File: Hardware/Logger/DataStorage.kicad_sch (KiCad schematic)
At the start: 10 parts, among them J6 112K-TAA0-RA1_ATTEND

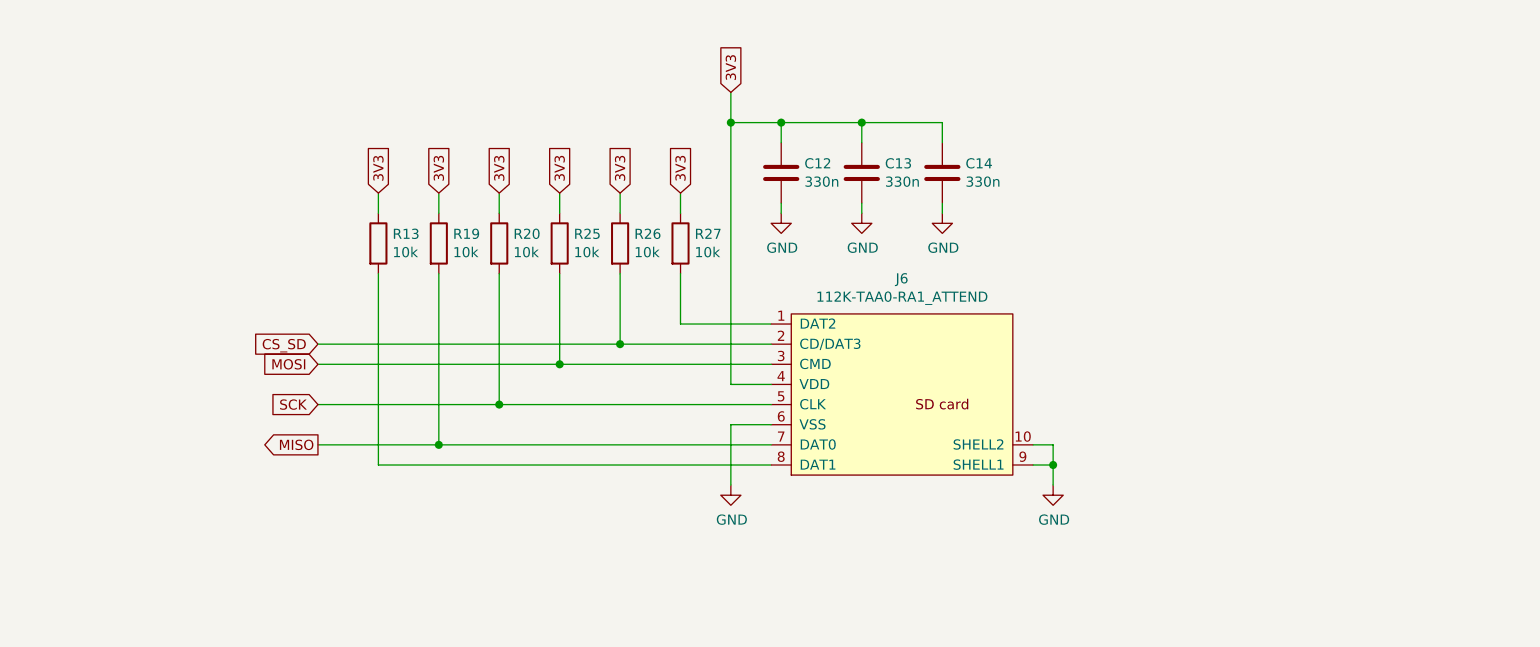
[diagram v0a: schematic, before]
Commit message: fixed SPI connections to SD card, added ESD protection for SD card
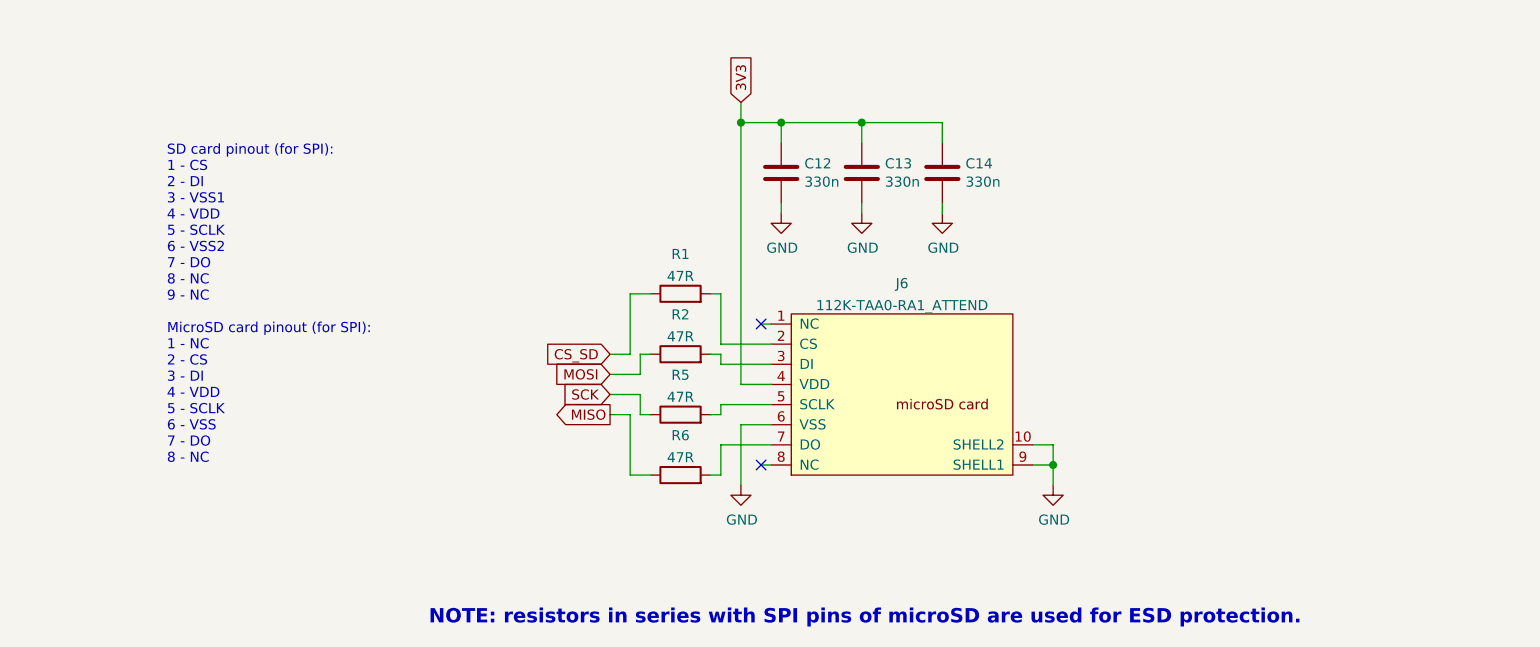
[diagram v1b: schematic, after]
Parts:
- removed R19, R20, R25, R26, R27: 10k, Resistor_SMD:R_0805_2012Metric, symbol Device:R
- added R2, R5, R6: 47R, Resistor_SMD:R_0805_2012Metric, symbol Device:R
- R1: renamed from R13; value 10k -> 47R
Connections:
- net 3V3: no longer R1.1
- net CS_SD: now also R1.1; no longer J6.2 (CD/DAT3)
- net MISO: now also R6.1; no longer J6.7 (DAT0)
- net MOSI: now also R2.1; no longer J6.3 (CMD)
- net SCK: now also R5.1; no longer J6.5 (CLK)
- net at R1.2: now also J6.2 (CS); no longer J6.8 (DAT1)
- new net: J6.3 (DI), R2.2
- new net: J6.5 (SCLK), R5.2
- new net: J6.7 (DO), R6.2
- no-connect marks 0 -> 2
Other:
- note added: "NOTE: resistors in series with SPI pins of microSD are used for ESD protection."
- note added: "SD card pinout (for SPI): 1 - CS 2 - DI 3 - VSS1 4 - VDD 5 - SCLK 6 - VSS2 7 - DO 8 - NC 9 - NC MicroSD card pinout (for SPI): 1 - NC 2 - CS 3 - DI 4 - VDD 5 - SCLK 6 - VSS 7 - DO 8 - NC"
- moved on the sheet: R1

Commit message: apply actual gpio connections to stm32 board, changed photoresistor to phototransistor
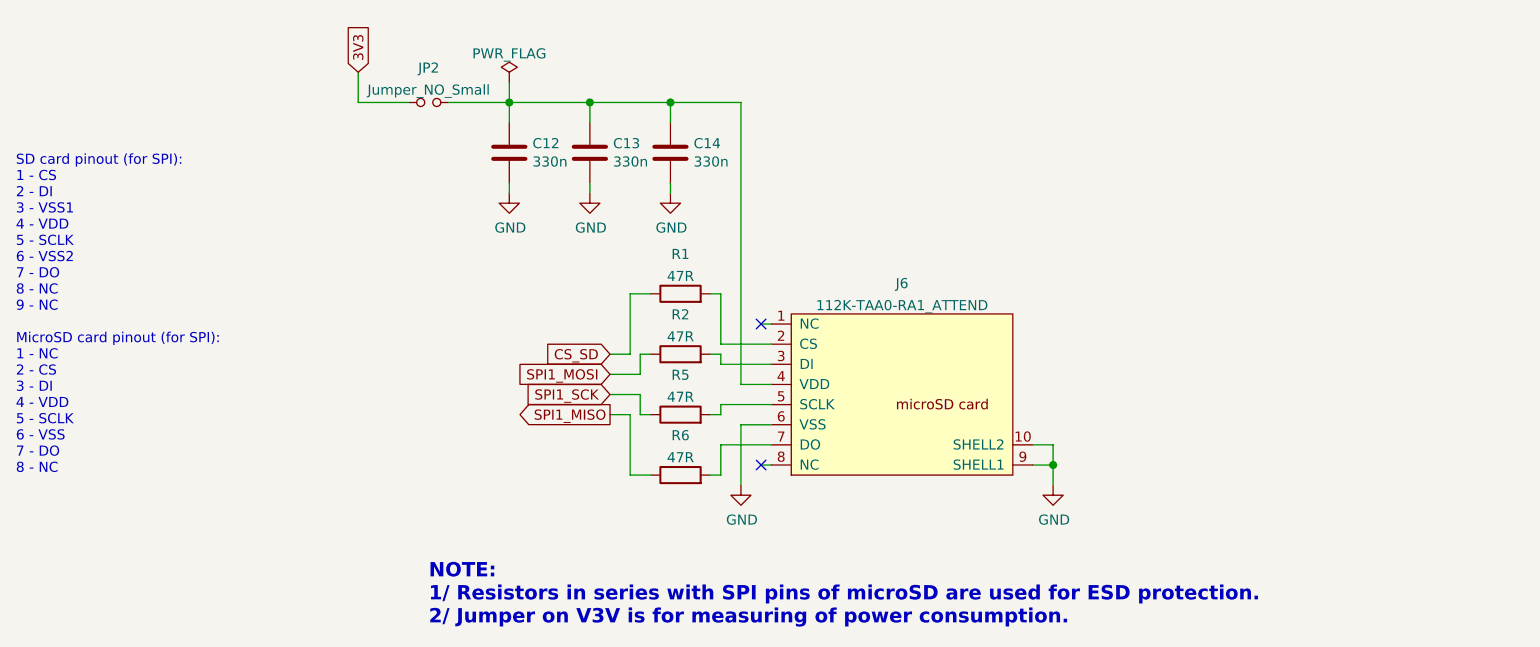
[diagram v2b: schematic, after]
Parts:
- added JP2: Jumper_NO_Small, symbol Device:Jumper_NO_Small
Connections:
- net 3V3: now also JP2.1; no longer C12.1, C13.1, C14.1, J6.4 (VDD)
- net MISO renamed SPI1_MISO
- net MOSI renamed SPI1_MOSI
- net SCK renamed SPI1_SCK
- new net: C12.1, C13.1, C14.1, J6.4 (VDD), JP2.2
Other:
- note added: "NOTE: 1/ Resistors in series with SPI pins of microSD are used for ESD protection. 2/ Jumper on V3V is for measuring of power consumption."
- note removed: "NOTE: resistors in series with SPI pins of microSD are used for ESD protection."
- moved on the sheet: C12, C13, C14

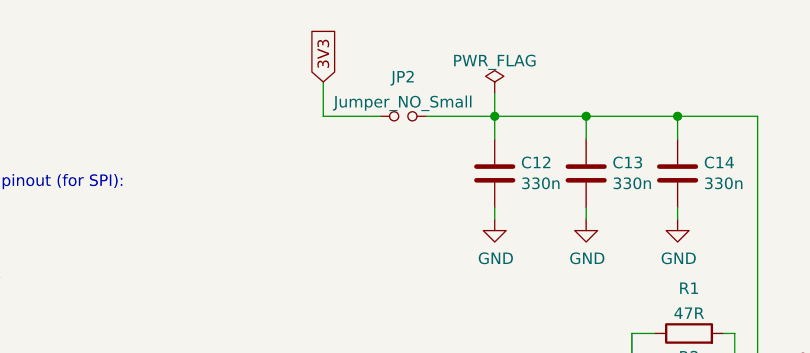
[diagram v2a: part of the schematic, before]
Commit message: draft of rev 3.0, cleanup of repo from not fully open source libs
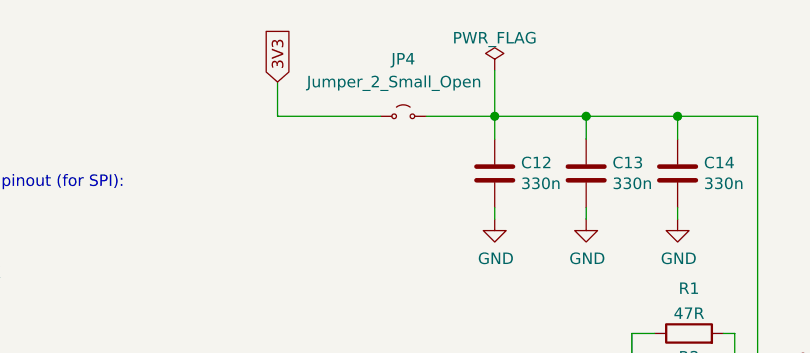
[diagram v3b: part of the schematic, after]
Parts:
- removed JP2: Jumper_NO_Small, symbol Device:Jumper_NO_Small
- added JP4: Jumper_2_Small_Open, Jumper:SolderJumper-2_P1.3mm_Open_TrianglePad1.0x1.5mm, symbol Jumper:Jumper_2_Small_Open
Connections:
- net 3V3: now also JP4.1 (A)
- net at C12.1, C13.1, C14.1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: now also JP4.2 (B)
